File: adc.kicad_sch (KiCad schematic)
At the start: 25 parts, among them J2 Conn_02x03_Odd_Even, U4 PCM1863DBT

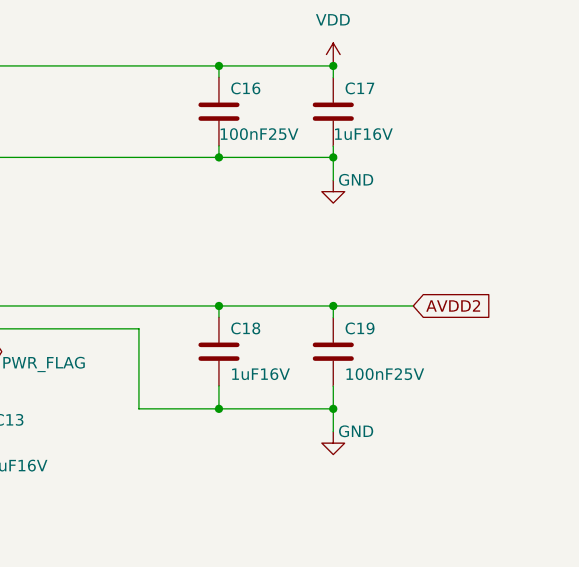
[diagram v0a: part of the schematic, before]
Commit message: Use Power Symbols for analog power
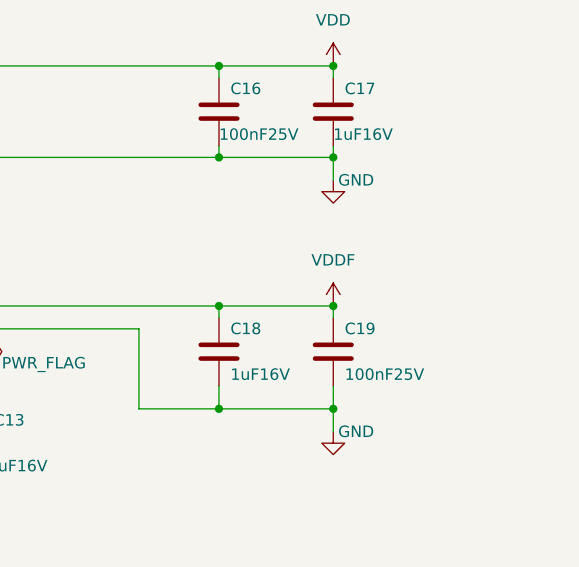
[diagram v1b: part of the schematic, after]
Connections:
- net AVDD2 renamed VDDF
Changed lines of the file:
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@@
   (junction (at 228.6 50.8) (diameter 0) (color 0 0 0 0)
   )
+  (junction (at 189.23 128.27) (diameter 0) (color 0 0 0 0)
+  )
+  (junction (at 228.6 67.31) (diameter 0) (color 0 0 0 0)
+  )
+  (junction (at 241.3 78.74) (diameter 0) (color 0 0 0 0)
+  )
+  (junction (at 165.1 139.7) (diameter 0) (color 0 0 0 0)
+  )
+  (junction (at 62.23 72.39) (diameter 0) (color 0 0 0 0)
+  )
+  (junction (at 201.93 72.39) (diameter 0) (color 0 0 0 0)
+  )
+  (junction (at 187.96 62.23) (diameter 0) (color 0 0 0 0)
+  )
+  (junction (at 228.6 40.64) (diameter 0) (color 0 0 0 0)
+  )
+  (junction (at 142.24 128.27) (diameter 0) (color 0 0 0 0)
+  )
+  (junction (at 62.23 74.93) (diameter 0) (color 0 0 0 0)
+  )
+  (junction (at 241.3 40.64) (diameter 0) (color 0 0 0 0)
+  )
+  (junction (at 172.72 139.7) (diameter 0) (color 0 0 0 0)
+  )
+  (junction (at 158.75 128.27) (diameter 0) (color 0 0 0 0)
+  )
+  (junction (at 241.3 50.8) (diameter 0) (color 0 0 0 0)
+  )
+  (junction (at 156.21 52.07) (diameter 0) (color 0 0 0 0)
+  )
+  (junction (at 158.75 139.7) (diameter 0) (color 0 0 0 0)
+  )
+  (junction (at 172.72 128.27) (diameter 0) (color 0 0 0 0)
+  )
   (junction (at 241.3 67.31) (diameter 0) (color 0 0 0 0)
-  )
-  (junction (at 189.23 128.27) (diameter 0) (color 0 0 0 0)
-  )
-  (junction (at 228.6 67.31) (diameter 0) (color 0 0 0 0)
-  )
-  (junction (at 241.3 78.74) (diameter 0) (color 0 0 0 0)
-  )
-  (junction (at 165.1 139.7) (diameter 0) (color 0 0 0 0)
-  )
-  (junction (at 62.23 72.39) (diameter 0) (color 0 0 0 0)
-  )
-  (junction (at 201.93 72.39) (diameter 0) (color 0 0 0 0)
-  )
-  (junction (at 187.96 62.23) (diameter 0) (color 0 0 0 0)
-  )
-  (junction (at 228.6 40.64) (diameter 0) (color 0 0 0 0)
-  )
-  (junction (at 142.24 128.27) (diameter 0) (color 0 0 0 0)
-  )
-  (junction (at 62.23 74.93) (diameter 0) (color 0 0 0 0)
-  )
-  (junction (at 241.3 40.64) (diameter 0) (color 0 0 0 0)
-  )
-  (junction (at 172.72 139.7) (diameter 0) (color 0 0 0 0)
-  )
-  (junction (at 158.75 128.27) (diameter 0) (color 0 0 0 0)
-  )
-  (junction (at 241.3 50.8) (diameter 0) (color 0 0 0 0)
-  )
-  (junction (at 156.21 52.07) (diameter 0) (color 0 0 0 0)
-  )
-  (junction (at 158.75 139.7) (diameter 0) (color 0 0 0 0)
-  )
-  (junction (at 172.72 128.27) (diameter 0) (color 0 0 0 0)
   )
   (junction (at 182.88 74.93) (diameter 0) (color 0 0 0 0)
@@
     (stroke (width 0) (type default))
   )
-  (wire (pts (xy 250.19 67.31) (xy 241.3 67.31))
-    (stroke (width 0) (type default))
-  )
   (wire (pts (xy 228.6 67.31) (xy 241.3 67.31))
     (stroke (width 0) (type default))
@@
     (property "Intersheetrefs" "${INTERSHEET_REFS}" (at 33.4104 54.61 0)
       (effects (font (size 1.27 1.27)) (justify right) hide)
-    )
-  )
-  (global_label "AVDD2" (shape input) (at 250.19 67.31 0)
-    (effects (font (size 1.27 1.27)) (justify left))
-    (property "Intersheetrefs" "${INTERSHEET_REFS}" (at 250.19 67.31 0)
-      (effects (font (size 1.27 1.27)) hide)
     )
   )
@@
         )
       )
+    )
+  )
+  (symbol (lib_id "power:VDDF") (at 241.3 67.31 0) (unit 1)
+    (in_bom yes) (on_board yes) (dnp no) (fields_autoplaced)
+    (property "Reference" "#PWR039" (at 241.3 71.12 0)
+      (effects (font (size 1.27 1.27)) hide)
+    )
+    (property "Value" "VDDF" (at 241.3 62.23 0)
+      (effects (font (size 1.27 1.27)))
+    )
+    (property "Footprint" "" (at 241.3 67.31 0)
+      (effects (font (size 1.27 1.27)) hide)
+    )
+    (property "Datasheet" "" (at 241.3 67.31 0)
+      (effects (font (size 1.27 1.27)) hide)
+    )
+    (pin "1")
+    (instances
+      (project "pedalboard-soundcard"
+        (path "/257597c6-fbef-4478-b0f4-968f2d6f1866/7494c0d8-b421-47d6-807b-2365bb2b2e5f"
+          (reference "#PWR039") (unit 1)
+        )
+      )

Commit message: Revert to standard RPI headers
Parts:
- J2: footprint Connector_PinHeader_2.54mm:PinHeader_2x03_P2.54mm_Vertical -> pedalboard-soundcard:PinSocket_2x03_P2.54mm_Vertical
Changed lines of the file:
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@@
       (effects (font (size 1.27 1.27)))
     )
-    (property "Footprint" "Connector_PinHeader_2.54mm:PinHeader_2x03_P2.54mm_Vertical" (at 238.76 137.16 0)
+    (property "Footprint" "pedalboard-soundcard:PinSocket_2x03_P2.54mm_Vertical" (at 238.76 137.16 0)
       (effects (font (size 1.27 1.27)) hide)
     )

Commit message: Fix library
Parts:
- U4: symbol zynthiandac-rescue:PCM1863DBT-pcm1863 -> pedalboard-soundcard:PCM1863DBT-pcm1863
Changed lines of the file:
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@@
     )
   )
-  (symbol (lib_id "zynthiandac-rescue:PCM1863DBT-pcm1863") (at 153.67 85.09 180) (unit 1)
+  (symbol (lib_id "pedalboard-soundcard:PCM1863DBT-pcm1863") (at 153.67 85.09 180) (unit 1)
     (in_bom yes) (on_board yes) (dnp no)
     (property "Reference" "U4" (at 113.03 94.9198 0)

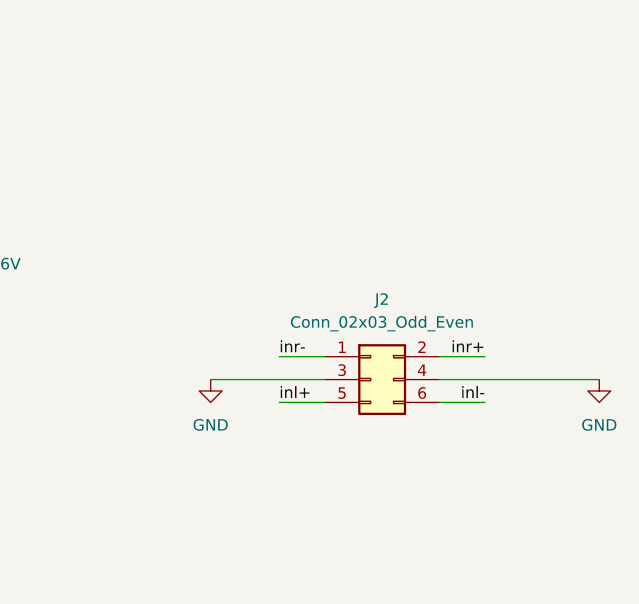
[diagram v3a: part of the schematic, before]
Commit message: Add 3.5mm jack connectors
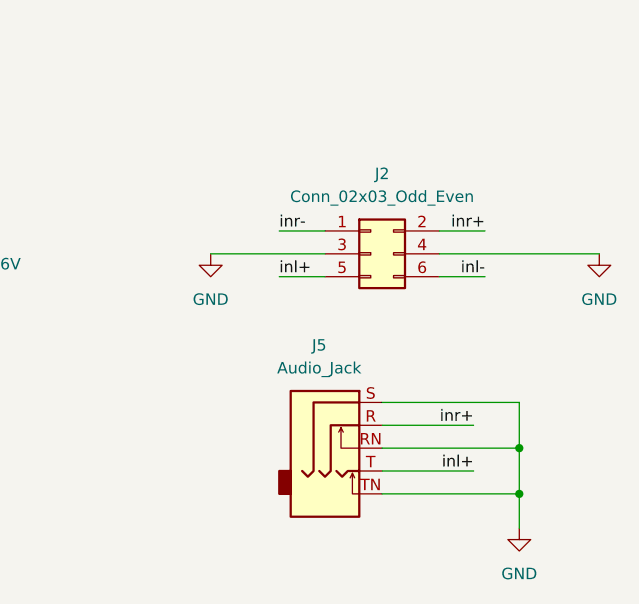
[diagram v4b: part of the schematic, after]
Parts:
- added J5: Audio_Jack, Connector_Audio:Jack_3.5mm_CUI_SJ1-3525N_Horizontal, symbol Connector_Audio:AudioJack3_SwitchTR
- J2: Supplier (none) -> https://www.digikey.ch/de/products/detail/te-connectivity-a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
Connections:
- net GND: now also J5.RN, J5.S, J5.TN
- net inl+: now also J5.T
- net inr+: now also J5.R
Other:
- moved on the sheet: J2

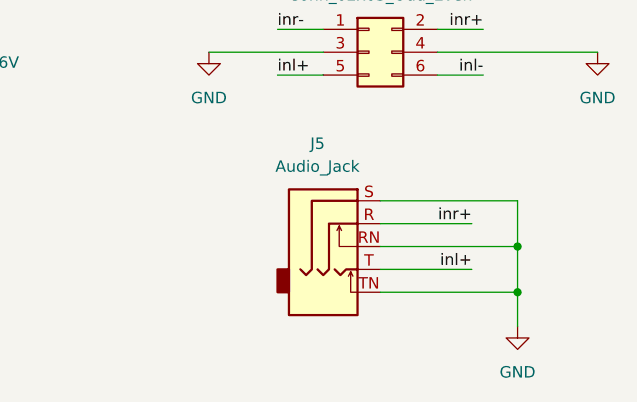
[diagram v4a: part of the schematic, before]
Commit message: DNP 3.5mm jack connectors
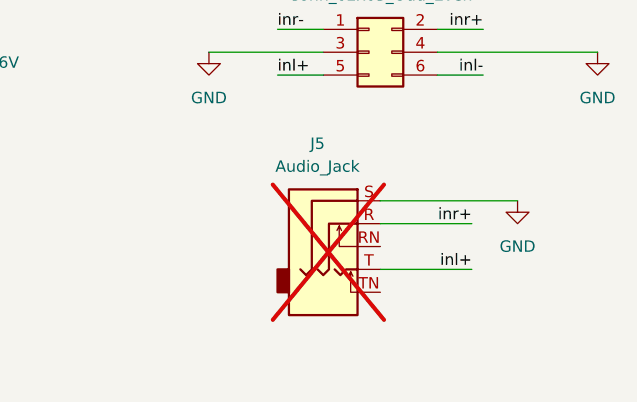
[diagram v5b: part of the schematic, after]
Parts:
- J5: now not fitted
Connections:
- net GND: no longer J5.RN, J5.TN
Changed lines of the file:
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@@
   (junction (at 228.6 67.31) (diameter 0) (color 0 0 0 0)
   )
-  (junction (at 255.27 149.86) (diameter 0) (color 0 0 0 0)
-  )
   (junction (at 241.3 78.74) (diameter 0) (color 0 0 0 0)
   )
@@
   )
   (junction (at 142.24 128.27) (diameter 0) (color 0 0 0 0)
-  )
-  (junction (at 255.27 144.78) (diameter 0) (color 0 0 0 0)
   )
   (junction (at 62.23 74.93) (diameter 0) (color 0 0 0 0)
@@
     (stroke (width 0) (type default))
   )
-  (wire (pts (xy 255.27 149.86) (xy 255.27 153.67))
-    (stroke (width 0) (type default))
-  )
-  (wire (pts (xy 255.27 144.78) (xy 255.27 149.86))
-    (stroke (width 0) (type default))
-  )
   (wire (pts (xy 240.03 147.32) (xy 250.19 147.32))
     (stroke (width 0) (type default))
@@
     (stroke (width 0) (type default))
   )
-  (wire (pts (xy 255.27 139.7) (xy 255.27 144.78))
-    (stroke (width 0) (type default))
-  )
   (wire (pts (xy 40.64 54.61) (xy 54.61 54.61))
     (stroke (width 0) (type default))
@@
     (stroke (width 0) (type default))
   )
-  (wire (pts (xy 240.03 144.78) (xy 255.27 144.78))
-    (stroke (width 0) (type default))
-  )
   (wire (pts (xy 228.6 67.31) (xy 241.3 67.31))
     (stroke (width 0) (type default))
@@
   )
   (wire (pts (xy 228.6 78.74) (xy 219.71 78.74))
-    (stroke (width 0) (type default))
-  )
-  (wire (pts (xy 240.03 149.86) (xy 255.27 149.86))
     (stroke (width 0) (type default))
   )
@@
     )
   )
-  (symbol (lib_id "power:GND") (at 255.27 153.67 0) (unit 1)
+  (symbol (lib_id "power:GND") (at 255.27 139.7 0) (unit 1)
     (in_bom yes) (on_board yes) (dnp no) (fields_autoplaced)
-    (property "Reference" "#PWR042" (at 255.27 160.02 0)
-      (effects (font (size 1.27 1.27)) hide)
-    )
-    (property "Value" "GND" (at 255.27 158.75 0)
-      (effects (font (size 1.27 1.27)))
-    )
-    (property "Footprint" "" (at 255.27 153.67 0)
-      (effects (font (size 1.27 1.27)) hide)
-    )
-    (property "Datasheet" "" (at 255.27 153.67 0)
+    (property "Reference" "#PWR042" (at 255.27 146.05 0)
+      (effects (font (size 1.27 1.27)) hide)
+    )
+    (property "Value" "GND" (at 255.27 144.78 0)
+      (effects (font (size 1.27 1.27)))
+    )
+    (property "Footprint" "" (at 255.27 139.7 0)
+      (effects (font (size 1.27 1.27)) hide)
+    )
+    (property "Datasheet" "" (at 255.27 139.7 0)
       (effects (font (size 1.27 1.27)) hide)
     )
@@
   )
   (symbol (lib_id "Connector_Audio:AudioJack3_SwitchTR") (at 234.95 142.24 0) (unit 1)
-    (in_bom yes) (on_board yes) (dnp no) (fields_autoplaced)
+    (in_bom yes) (on_board yes) (dnp yes) (fields_autoplaced)
     (property "Reference" "J5" (at 233.045 133.35 0)
       (effects (font (size 1.27 1.27)))

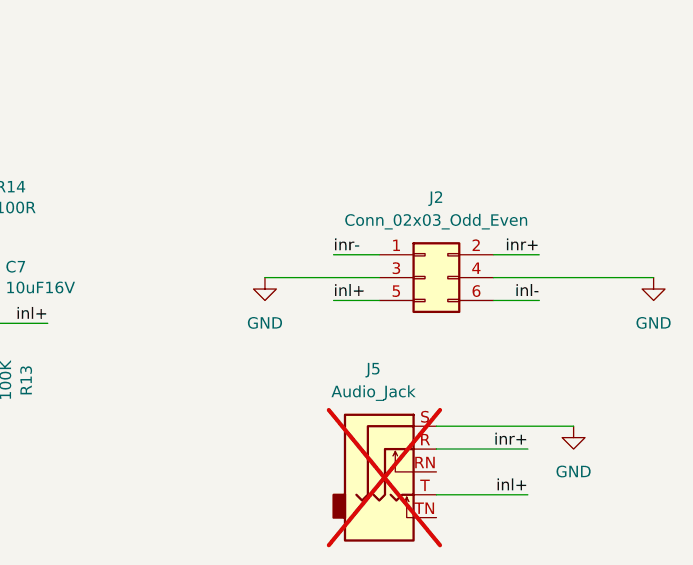
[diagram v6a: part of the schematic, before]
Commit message: Add panel tabs
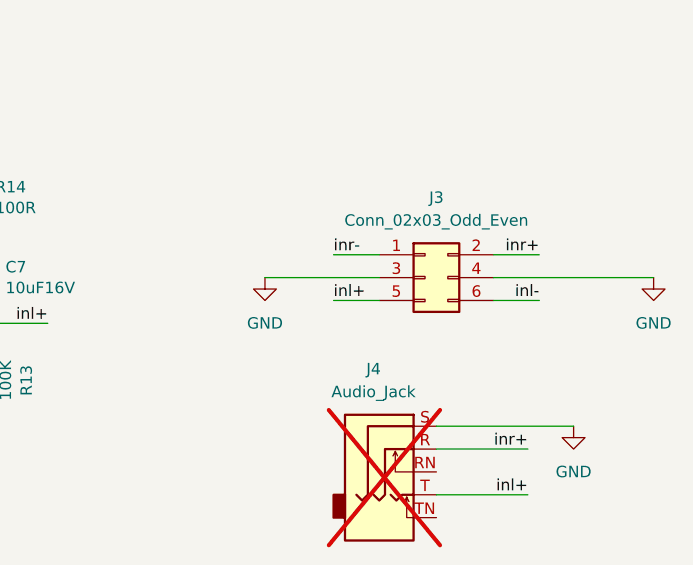
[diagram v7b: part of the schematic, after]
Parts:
- renumbered J2 to J3, J5 to J4
